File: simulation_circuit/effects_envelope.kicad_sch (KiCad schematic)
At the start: 16 parts, among them Q1 BC547

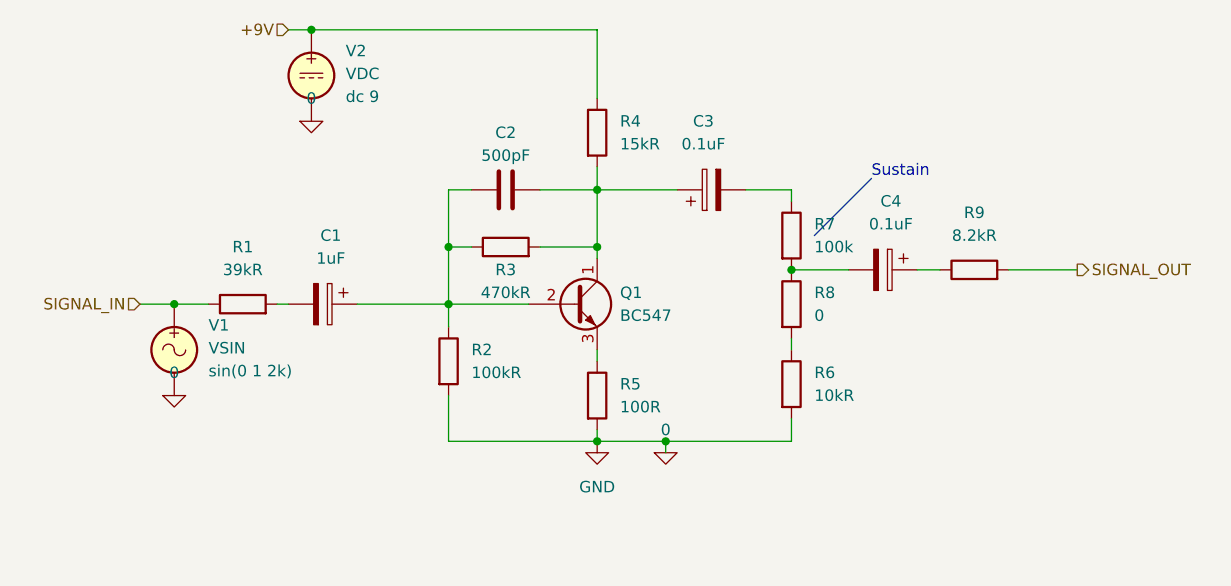
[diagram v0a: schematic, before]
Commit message: added LTSpice standard diode library to SPICE sim library, copied and simulated envelope effect, WIP determining if isolated or chained sim behaviour is correct
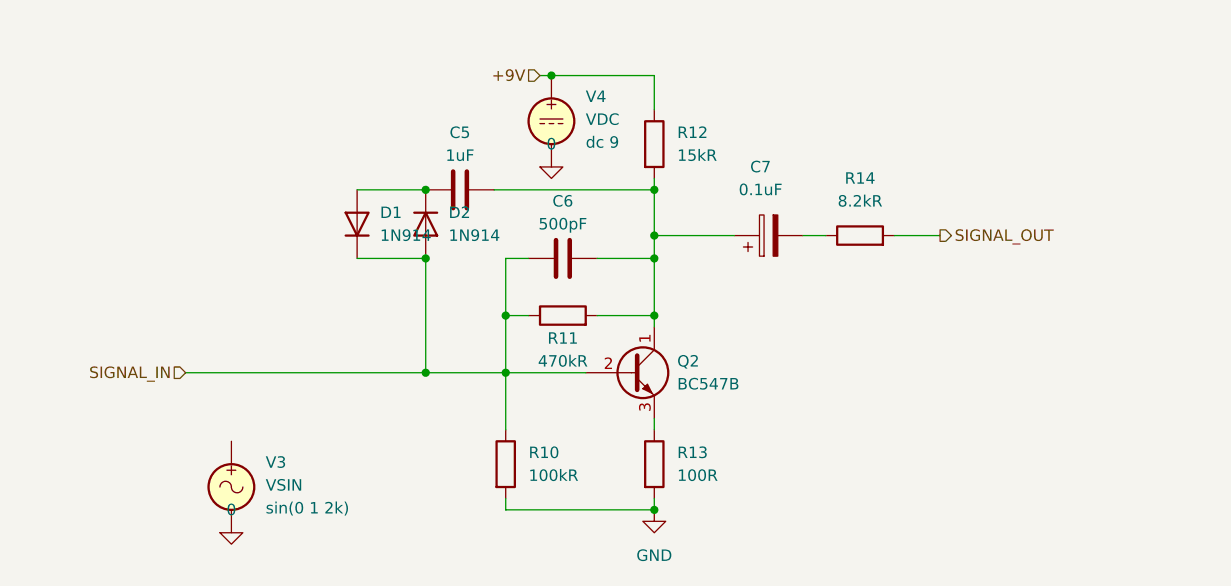
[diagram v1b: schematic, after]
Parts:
- removed C1: 1uF, symbol Device:C_Polarized
- removed C2: 500pF, symbol Device:C
- removed C3, C4: 0.1uF, symbol Device:C_Polarized
- removed Q1: BC547, Package_TO_SOT_THT:TO-92_Inline, symbol Transistor_BJT:BC547
- removed R1: 39kR, symbol Device:R
- removed R2: 100kR, symbol Device:R
- removed R3: 470kR, symbol Device:R
- removed R4: 15kR, symbol Device:R
- removed R5: 100R, symbol Device:R
- removed R6: 10kR, symbol Device:R
- removed R7: 100k, symbol Device:R
- removed R8: 0, symbol Device:R
- removed R9: 8.2kR, symbol Device:R
- removed V1: VSIN, symbol Simulation_SPICE:VSIN
- removed V2: VDC, symbol Simulation_SPICE:VDC
- added C5: 1uF, symbol Device:C
- added C6: 500pF, symbol Device:C
- added C7: 0.1uF, symbol Device:C_Polarized
- added D1, D2: 1N914, Diode_THT:D_DO-35_SOD27_P7.62mm_Horizontal, symbol Device:D
- added Q2: BC547B, Package_TO_SOT_THT:TO-92_Inline, symbol Transistor_BJT:BC547
- added R10: 100kR, symbol Device:R
- added R11: 470kR, symbol Device:R
- added R12: 15kR, symbol Device:R
- added R13: 100R, symbol Device:R
- added R14: 8.2kR, symbol Device:R
- added V3: VSIN, symbol Simulation_SPICE:VSIN
- added V4: VDC, symbol Simulation_SPICE:VDC
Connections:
- net +9V: now also R12.1, V4.1
- net 0: now also V3.2, V4.2
- net SIGNAL_IN: now also C6.1, D1.1 (K), D2.2 (A), Q2.2 (B), R10.1, R11.1
- net SIGNAL_OUT: now also R14.2
- new net: C5.2, C6.2, C7.1, Q2.1 (C), R11.2, R12.2
- new net: Q2.3 (E), R13.1
- new net: C7.2, R14.1
- new net: C5.1, D1.2 (A), D2.1 (K)
- new net GND: R10.2, R13.2
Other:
- note removed: "Sustain"

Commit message: WIP
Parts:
- removed V4: VDC, symbol Simulation_SPICE:VDC
- V3: Spice_Model sin(0 1 2k) -> sin(0 0.5 440)
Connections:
- net GND is gone; now on net 0: R10.2, R13.2
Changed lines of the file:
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@@
   (junction (at 154.94 95.25) (diameter 0) (color 0 0 0 0)
   )
+  (junction (at 147.32 116.84) (diameter 0) (color 0 0 0 0)
+  )
   (junction (at 129.54 88.9) (diameter 0) (color 0 0 0 0)
   )
@@
   (junction (at 154.94 86.36) (diameter 0) (color 0 0 0 0)
   )
-  (junction (at 143.51 68.58) (diameter 0) (color 0 0 0 0)
-  )
   (junction (at 154.94 81.28) (diameter 0) (color 0 0 0 0)
   )
@@
     (stroke (width 0) (type default) (color 0 0 0 0))
   )
-  (wire (pts (xy 143.51 68.58) (xy 154.94 68.58))
+  (wire (pts (xy 142.24 68.58) (xy 154.94 68.58))
     (stroke (width 0) (type default) (color 0 0 0 0))
   )
@@
     (stroke (width 0) (type default) (color 0 0 0 0))
   )
+  (wire (pts (xy 147.32 116.84) (xy 154.94 116.84))
+    (stroke (width 0) (type default) (color 0 0 0 0))
+  )
   (wire (pts (xy 154.94 106.68) (xy 154.94 107.95))
     (stroke (width 0) (type default) (color 0 0 0 0))
   )
+  (wire (pts (xy 102.87 101.6) (xy 129.54 101.6))
+    (stroke (width 0) (type default) (color 0 0 0 0))
+  )
   (wire (pts (xy 154.94 72.39) (xy 154.94 68.58))
     (stroke (width 0) (type default) (color 0 0 0 0))
@@
     (stroke (width 0) (type default) (color 0 0 0 0))
   )
-  (wire (pts (xy 102.87 101.6) (xy 129.54 101.6))
+  (wire (pts (xy 147.32 116.84) (xy 147.32 118.11))
     (stroke (width 0) (type default) (color 0 0 0 0))
   )
@@
     (stroke (width 0) (type default) (color 0 0 0 0))
   )
-  (wire (pts (xy 138.43 116.84) (xy 154.94 116.84))
+  (wire (pts (xy 138.43 116.84) (xy 147.32 116.84))
     (stroke (width 0) (type default) (color 0 0 0 0))
   )
@@
   )
   (wire (pts (xy 154.94 86.36) (xy 154.94 88.9))
-    (stroke (width 0) (type default) (color 0 0 0 0))
-  )
-  (wire (pts (xy 142.24 68.58) (xy 143.51 68.58))
     (stroke (width 0) (type default) (color 0 0 0 0))
   )
@@
   (symbol (lib_id "power:GND") (at 154.94 116.84 0) (unit 1)
     (in_bom yes) (on_board yes) (fields_autoplaced)
-    (property "Reference" "#PWR?" (id 0) (at 154.94 123.19 0)
+    (property "Reference" "#PWR0101" (id 0) (at 154.94 123.19 0)
       (effects (font (size 1.27 1.27)) hide)
     )
@@
   (symbol (lib_id "pspice:0") (at 107.95 119.38 0) (unit 1)
     (in_bom yes) (on_board yes) (fields_autoplaced)
-    (property "Reference" "#GND?" (id 0) (at 107.95 121.92 0)
+    (property "Reference" "#GND0101" (id 0) (at 107.95 121.92 0)
       (effects (font (size 1.27 1.27)) hide)
     )
@@
     (pin "2")
   )
-  (symbol (lib_id "pspice:0") (at 143.51 78.74 0) (unit 1)
-    (in_bom yes) (on_board yes) (fields_autoplaced)
-    (property "Reference" "#GND?" (id 0) (at 143.51 81.28 0)
-      (effects (font (size 1.27 1.27)) hide)
-    )
-    (property "Value" "0" (id 1) (at 143.51 76.2 0))
-    (property "Footprint" "" (id 2) (at 143.51 78.74 0)
-      (effects (font (size 1.27 1.27)) hide)
-    )
-    (property "Datasheet" "~" (id 3) (at 143.51 78.74 0)
+  (symbol (lib_id "pspice:0") (at 147.32 118.11 0) (unit 1)
+    (in_bom yes) (on_board yes) (fields_autoplaced)
+    (property "Reference" "#GND0102" (id 0) (at 147.32 120.65 0)
+      (effects (font (size 1.27 1.27)) hide)
+    )
+    (property "Value" "0" (id 1) (at 147.32 115.57 0))
+    (property "Footprint" "" (id 2) (at 147.32 118.11 0)
+      (effects (font (size 1.27 1.27)) hide)
+    )
+    (property "Datasheet" "~" (id 3) (at 147.32 118.11 0)
       (effects (font (size 1.27 1.27)) hide)
     )
@@
     (pin "2")
   )
-  (symbol (lib_id "Simulation_SPICE:VDC") (at 143.51 73.66 0) (unit 1)
-    (in_bom yes) (on_board yes) (fields_autoplaced)
-    (property "Reference" "V4" (id 0) (at 147.32 70.9301 0)
-      (effects (font (size 1.27 1.27)) (justify left))
-    )
-    (property "Value" "VDC" (id 1) (at 147.32 73.4701 0)
-      (effects (font (size 1.27 1.27)) (justify left))
-    )
-    (property "Footprint" "" (id 2) (at 143.51 73.66 0)
-      (effects (font (size 1.27 1.27)) hide)
-    )
-    (property "Datasheet" "~" (id 3) (at 143.51 73.66 0)
-      (effects (font (size 1.27 1.27)) hide)
-    )
-    (property "Spice_Netlist_Enabled" "Y" (id 4) (at 143.51 73.66 0)
-      (effects (font (size 1.27 1.27)) (justify left) hide)
-    )
-    (property "Spice_Primitive" "V" (id 5) (at 143.51 73.66 0)
-      (effects (font (size 1.27 1.27)) (justify left) hide)
-    )
-    (property "Spice_Model" "dc 9" (id 6) (at 147.32 76.0101 0)
-      (effects (font (size 1.27 1.27)) (justify left))
-    )
-    (pin "1")
-    (pin "2")
-  )
   (symbol (lib_id "Device:C_Polarized") (at 167.64 86.36 90) (unit 1)
     (in_bom yes) (on_board yes) (fields_autoplaced)
@@
       (effects (font (size 1.27 1.27)) (justify left) hide)
     )
-    (property "Spice_Model" "sin(0 1 2k)" (id 6) (at 111.76 116.6501 0)
-      (effects (font (size 1.27 1.27)) (justify left))
-    )
+    (property "Spice_Model" "sin(0 0.5 440)" (id 6) (at 111.76 116.6501 0)
+      (effects (font (size 1.27 1.27)) (justify left))
+    )
